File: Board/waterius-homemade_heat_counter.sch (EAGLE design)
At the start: 38 parts, among them IC1 TINY13-20SU, Q1 MMBTA92, Q2 MMBTA92, U1 RS-485-MODULE

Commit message: rewire1
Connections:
- net +3V3: no longer Q2.E, R15.1
- net AA*3: now also Q2.E, R15.1
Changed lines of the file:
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@@
 <attribute name="OM" value="3k6"/>
 </part>
-<part name="+3V6" library="supply1" library_urn="urn:adsk.eagle:library:371" deviceset="+3V3" device=""/>
 <part name="JP7" library="pinhead" library_urn="urn:adsk.eagle:library:325" deviceset="PINHD-1X2" device="" package3d_urn="urn:adsk.eagle:package:22435/2" value="DC_StepUp_Power"/>
 <part name="JP8" library="pinhead" library_urn="urn:adsk.eagle:library:325" deviceset="PINHD-1X2" device="" package3d_urn="urn:adsk.eagle:package:22435/2" value="DC_IN_9V"/>
@@
 <instance part="+3V3" gate="G$1" x="53.848" y="69.088" smashed="yes"/>
 <instance part="+3V4" gate="G$1" x="48.514" y="69.088" smashed="yes"/>
-<instance part="R4" gate="G$1" x="61.722" y="26.924" smashed="yes" rot="R270">
-<attribute name="VALUE" x="62.484" y="22.098" size="1.778" layer="96"/>
-</instance>
-<instance part="LED1" gate="G$1" x="61.722" y="39.116" smashed="yes">
-<attribute name="VALUE" x="62.103" y="35.052" size="1.778" layer="96" rot="R180"/>
+<instance part="R4" gate="G$1" x="61.722" y="24.384" smashed="yes" rot="R270">
+<attribute name="VALUE" x="62.484" y="19.558" size="1.778" layer="96"/>
+</instance>
+<instance part="LED1" gate="G$1" x="61.722" y="36.576" smashed="yes">
+<attribute name="VALUE" x="62.103" y="32.512" size="1.778" layer="96" rot="R180"/>
 </instance>
 <instance part="+3V8" gate="G$1" x="-9.906" y="76.2" smashed="yes">
@@
 <attribute name="NAME" x="-20.828" y="95.2246" size="1.778" layer="95" rot="R90"/>
 <attribute name="VALUE" x="-23.622" y="94.996" size="1.778" layer="96" rot="R90"/>
-</instance>
-<instance part="+3V6" gate="G$1" x="-5.334" y="119.888" smashed="yes">
-<attribute name="VALUE" x="-7.874" y="117.348" size="1.778" layer="96" rot="R180"/>
 </instance>
 <instance part="JP7" gate="G$1" x="-61.214" y="67.31" smashed="yes">
@@
 <segment>
 <pinref part="R4" gate="G$1" pin="2"/>
-<wire x1="61.722" y1="21.844" x2="61.722" y2="18.542" width="0.1524" layer="91"/>
+<wire x1="61.722" y1="19.304" x2="61.722" y2="18.542" width="0.1524" layer="91"/>
 <pinref part="GND3" gate="1" pin="GND"/>
 </segment>
@@
 </segment>
 <segment>
-<pinref part="JP5" gate="A" pin="3"/>
-<wire x1="75.438" y1="65.278" x2="75.438" y2="66.04" width="0.1524" layer="91"/>
 <pinref part="GND8" gate="1" pin="GND"/>
-<wire x1="75.692" y1="58.928" x2="75.692" y2="66.04" width="0.1524" layer="91"/>
-<wire x1="75.692" y1="66.04" x2="75.438" y2="66.04" width="0.1524" layer="91"/>
-<junction x="75.438" y="66.04"/>
 <pinref part="JP2" gate="G$1" pin="2"/>
 <wire x1="75.692" y1="58.928" x2="90.678" y2="58.928" width="0.1524" layer="91"/>
 <wire x1="90.678" y1="58.928" x2="90.678" y2="66.548" width="0.1524" layer="91"/>
+<pinref part="JP5" gate="A" pin="3"/>
+<wire x1="75.438" y1="65.278" x2="75.438" y2="66.04" width="0.1524" layer="91"/>
+<wire x1="75.438" y1="66.04" x2="75.438" y2="58.928" width="0.1524" layer="91"/>
+<wire x1="75.438" y1="58.928" x2="75.692" y2="58.928" width="0.1524" layer="91"/>
+<junction x="75.438" y="66.04"/>
 <junction x="75.692" y="58.928"/>
 </segment>
@@
 <label x="176.53" y="87.376" size="1.778" layer="95"/>
 </segment>
-<segment>
-<pinref part="Q2" gate="G$1" pin="E"/>
-<wire x1="-5.334" y1="105.664" x2="-5.334" y2="113.284" width="0.1524" layer="91"/>
-<pinref part="R15" gate="G$1" pin="1"/>
-<wire x1="-5.334" y1="113.284" x2="-5.334" y2="115.316" width="0.1524" layer="91"/>
-<wire x1="-13.97" y1="113.284" x2="-5.334" y2="113.284" width="0.1524" layer="91"/>
-<junction x="-5.334" y="113.284"/>
-<pinref part="+3V6" gate="G$1" pin="+3V3"/>
-<wire x1="-5.334" y1="117.348" x2="-5.334" y2="113.284" width="0.1524" layer="91"/>
-</segment>
 </net>
 <net name="AVR_RST" class="0">
@@
 <label x="-41.402" y="115.57" size="1.778" layer="95"/>
 </segment>
+<segment>
+<pinref part="Q2" gate="G$1" pin="E"/>
+<wire x1="-5.334" y1="105.664" x2="-5.334" y2="113.284" width="0.1524" layer="91"/>
+<pinref part="R15" gate="G$1" pin="1"/>
+<wire x1="-5.334" y1="113.284" x2="-5.334" y2="115.316" width="0.1524" layer="91"/>
+<wire x1="-13.97" y1="113.284" x2="-5.334" y2="113.284" width="0.1524" layer="91"/>
+<junction x="-5.334" y="113.284"/>
+<label x="-5.08" y="114.3" size="1.778" layer="95"/>
+</segment>
 </net>
 <net name="N$3" class="0">
@@
 <pinref part="LED1" gate="G$1" pin="A"/>
 <pinref part="U$3" gate="G$1" pin="TX"/>
-<wire x1="61.722" y1="50.292" x2="61.722" y2="41.656" width="0.1524" layer="91"/>
+<wire x1="61.722" y1="50.292" x2="61.722" y2="39.116" width="0.1524" layer="91"/>
 <wire x1="35.052" y1="50.292" x2="61.722" y2="50.292" width="0.1524" layer="91"/>
 <junction x="61.722" y="50.292"/>
@@
 <segment>
 <pinref part="LED1" gate="G$1" pin="C"/>
-<wire x1="61.722" y1="34.036" x2="61.722" y2="32.004" width="0.1524" layer="91"/>
+<wire x1="61.722" y1="31.496" x2="61.722" y2="29.464" width="0.1524" layer="91"/>
 <pinref part="R4" gate="G$1" pin="1"/>
 </segment>
@@
 </sheet>
 </sheets>
-<errors>
-</errors>
 </schematic>
 </drawing>

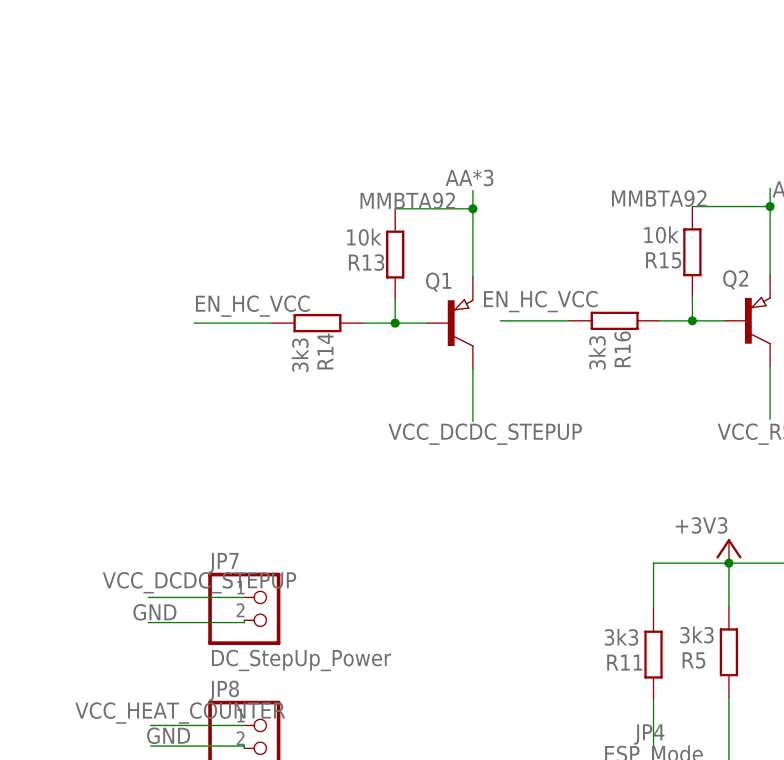
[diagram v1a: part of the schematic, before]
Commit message: remove 1 trans
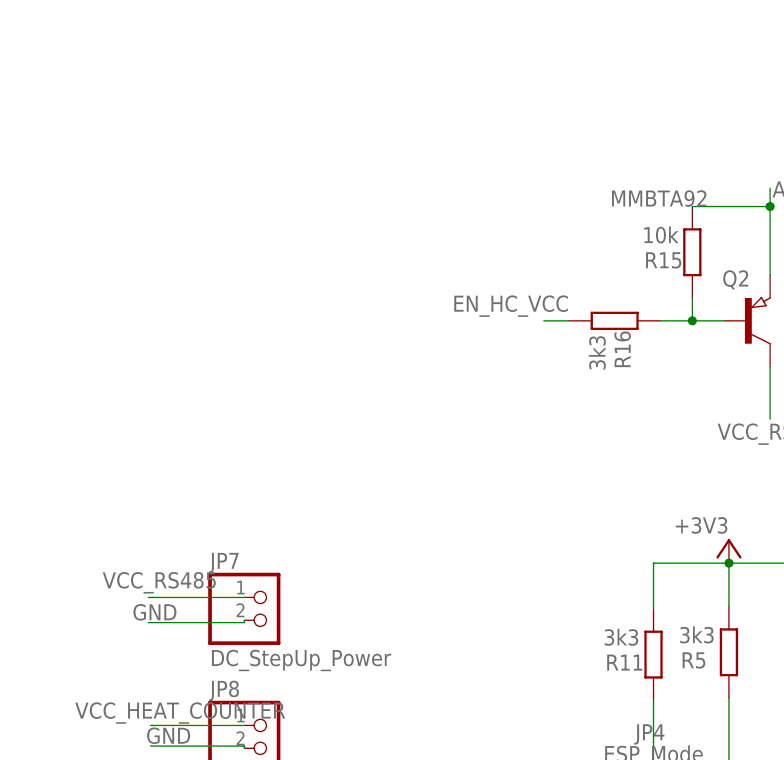
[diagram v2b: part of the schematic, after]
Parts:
- removed Q1: MMBTA92, semicon-smd-ipc:PNP-TRANSISTOR_SOT23
- removed R13: 10k, rcl:R-EU_R0805
- removed R14: 3k3, rcl:R-EU_R0805
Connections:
- removed net N$10: Q1.B, R13.2, R14.2
- removed net VCC_DCDC_STEPUP: JP7.1, Q1.C
- net AA*3: no longer Q1.E, R13.1
- net EN_HC_VCC: no longer R14.1
- net VCC_RS485: now also JP7.1
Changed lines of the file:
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@@
 <part name="JP6" library="pinhead" library_urn="urn:adsk.eagle:library:325" deviceset="PINHD-2X5" device="" package3d_urn="urn:adsk.eagle:package:22470/2" value="AVR_PROG"/>
 <part name="JP4" library="pinhead" library_urn="urn:adsk.eagle:library:325" deviceset="PINHD-1X3" device="" package3d_urn="urn:adsk.eagle:package:22458/2" value="ESP_Mode"/>
-<part name="Q1" library="semicon-smd-ipc" library_urn="urn:adsk.eagle:library:353" deviceset="PNP-TRANSISTOR_" device="SOT23" package3d_urn="urn:adsk.eagle:package:28738/2" value="MMBTA92"/>
-<part name="R13" library="rcl" deviceset="R-EU_" device="R0805" value="10k">
-<attribute name="OM" value="3k6"/>
-</part>
-<part name="R14" library="rcl" deviceset="R-EU_" device="R0805" value="3k3">
-<attribute name="OM" value="3k6"/>
-</part>
 <part name="Q2" library="semicon-smd-ipc" library_urn="urn:adsk.eagle:library:353" deviceset="PNP-TRANSISTOR_" device="SOT23" package3d_urn="urn:adsk.eagle:package:28738/2" value="MMBTA92"/>
 <part name="R15" library="rcl" deviceset="R-EU_" device="R0805" value="10k">
@@
 <attribute name="VALUE" x="-23.876" y="51.562" size="1.778" layer="96"/>
 </instance>
-<instance part="Q1" gate="G$1" x="-40.894" y="100.33" smashed="yes">
-<attribute name="NAME" x="-43.688" y="104.14" size="1.778" layer="95"/>
-<attribute name="VALUE" x="-51.054" y="113.03" size="1.778" layer="96"/>
-</instance>
-<instance part="R13" gate="G$1" x="-46.99" y="107.95" smashed="yes" rot="R270">
-<attribute name="NAME" x="-52.3494" y="106.172" size="1.778" layer="95"/>
-<attribute name="VALUE" x="-52.578" y="108.966" size="1.778" layer="96"/>
-</instance>
-<instance part="R14" gate="G$1" x="-55.626" y="100.33" smashed="yes">
-<attribute name="NAME" x="-53.848" y="94.9706" size="1.778" layer="95" rot="R90"/>
-<attribute name="VALUE" x="-56.642" y="94.742" size="1.778" layer="96" rot="R90"/>
-</instance>
 <instance part="Q2" gate="G$1" x="-7.874" y="100.584" smashed="yes">
 <attribute name="NAME" x="-10.668" y="104.394" size="1.778" layer="95"/>
@@
 </segment>
 <segment>
-<pinref part="Q1" gate="G$1" pin="E"/>
-<wire x1="-38.354" y1="105.41" x2="-38.354" y2="113.03" width="0.1524" layer="91"/>
-<pinref part="R13" gate="G$1" pin="1"/>
-<wire x1="-38.354" y1="113.03" x2="-38.354" y2="115.062" width="0.1524" layer="91"/>
-<wire x1="-46.99" y1="113.03" x2="-38.354" y2="113.03" width="0.1524" layer="91"/>
-<junction x="-38.354" y="113.03"/>
-<label x="-41.402" y="115.57" size="1.778" layer="95"/>
-</segment>
-<segment>
 <pinref part="Q2" gate="G$1" pin="E"/>
 <wire x1="-5.334" y1="105.664" x2="-5.334" y2="113.284" width="0.1524" layer="91"/>
@@
 </segment>
 </net>
-<net name="N$10" class="0">
-<segment>
-<pinref part="Q1" gate="G$1" pin="B"/>
-<pinref part="R14" gate="G$1" pin="2"/>
-<wire x1="-43.434" y1="100.33" x2="-46.99" y2="100.33" width="0.1524" layer="91"/>
-<pinref part="R13" gate="G$1" pin="2"/>
-<wire x1="-46.99" y1="100.33" x2="-50.546" y2="100.33" width="0.1524" layer="91"/>
-<wire x1="-46.99" y1="102.87" x2="-46.99" y2="100.33" width="0.1524" layer="91"/>
-<junction x="-46.99" y="100.33"/>
-</segment>
-</net>
-<net name="VCC_DCDC_STEPUP" class="0">
-<segment>
-<pinref part="Q1" gate="G$1" pin="C"/>
-<wire x1="-38.354" y1="95.25" x2="-38.354" y2="89.408" width="0.1524" layer="91"/>
-<label x="-47.752" y="87.376" size="1.778" layer="95"/>
-</segment>
-<segment>
-<pinref part="JP7" gate="G$1" pin="1"/>
-<wire x1="-63.754" y1="69.85" x2="-74.422" y2="69.85" width="0.1524" layer="91"/>
-<label x="-79.502" y="70.866" size="1.778" layer="95"/>
-</segment>
-</net>
 <net name="N$13" class="0">
 <segment>
@@
 <label x="-88.9" y="27.94" size="1.778" layer="95"/>
 </segment>
+<segment>
+<pinref part="JP7" gate="G$1" pin="1"/>
+<wire x1="-63.754" y1="69.85" x2="-74.422" y2="69.85" width="0.1524" layer="91"/>
+<label x="-79.502" y="70.866" size="1.778" layer="95"/>
+</segment>
 </net>
 <net name="EN_HC_VCC" class="0">
-<segment>
-<pinref part="R14" gate="G$1" pin="1"/>
-<wire x1="-60.706" y1="100.33" x2="-69.342" y2="100.33" width="0.1524" layer="91"/>
-<label x="-69.342" y="101.6" size="1.778" layer="95"/>
-</segment>
-<segment>
-<pinref part="R16" gate="G$1" pin="1"/>
-<wire x1="-27.686" y1="100.584" x2="-35.306" y2="100.584" width="0.1524" layer="91"/>
-<label x="-37.338" y="102.108" size="1.778" layer="95"/>
-</segment>
 <segment>
 <pinref part="U$3" gate="G$1" pin="GPIO12"/>
@@
 <label x="-11.43" y="38.1" size="1.778" layer="95"/>
 </segment>
-</net>
+<segment>
+<pinref part="R16" gate="G$1" pin="1"/>
+<wire x1="-27.686" y1="100.584" x2="-30.48" y2="100.584" width="0.1524" layer="91"/>
+<label x="-40.64" y="101.6" size="1.778" layer="95"/>
+</segment>
+</net>
